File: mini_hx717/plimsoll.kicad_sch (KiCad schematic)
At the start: 17 parts, among them J1 Conn_02x06_Odd_Even, J3 Loadd Cell, U5 RS3236-3.3, U6 HX717

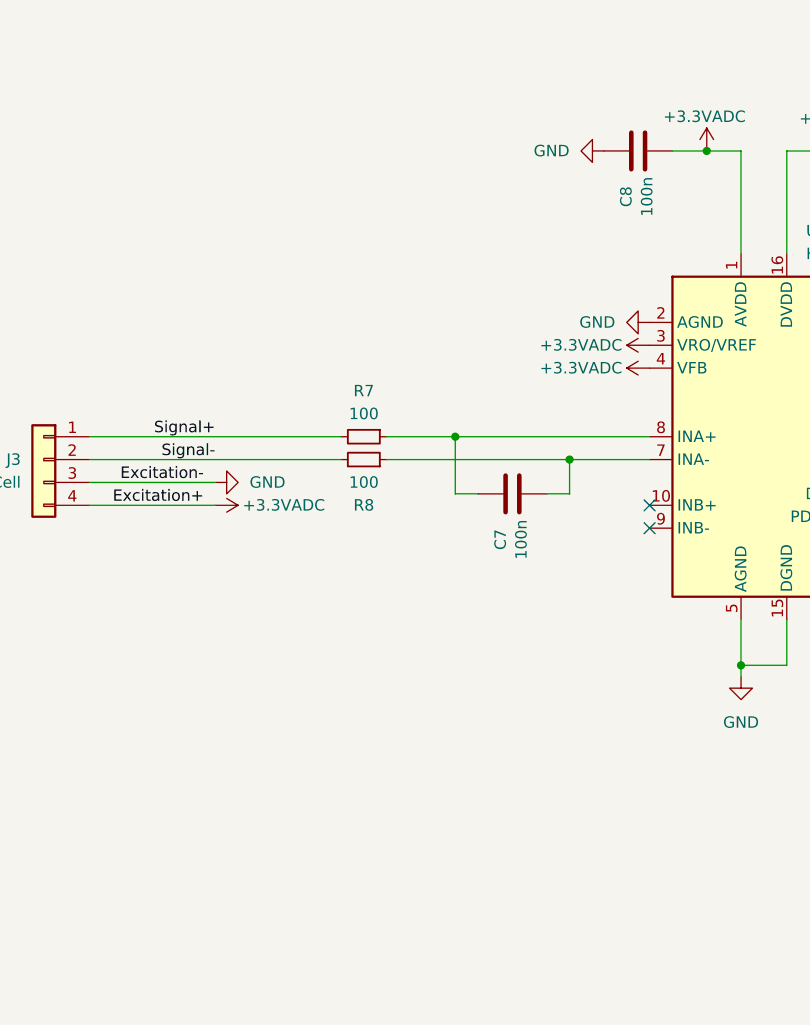
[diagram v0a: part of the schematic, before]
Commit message: ads1220 added
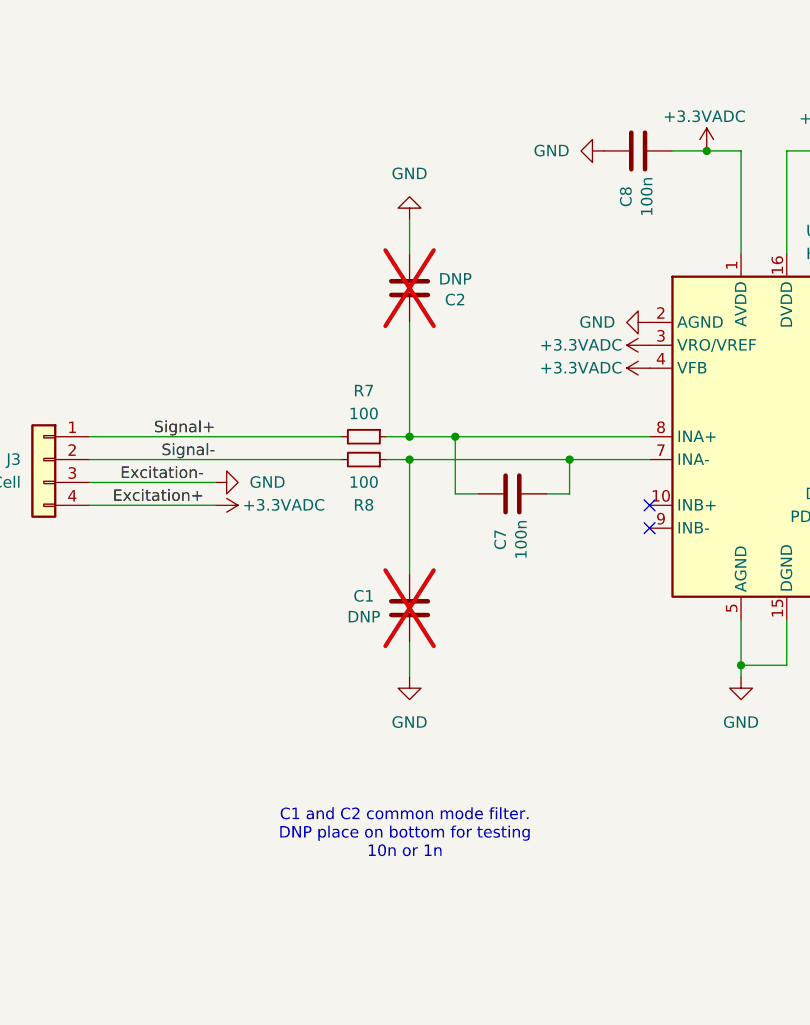
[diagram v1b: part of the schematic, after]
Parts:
- added C1, C2: DNP, Capacitor_SMD:C_0603_1608Metric, symbol Device:C
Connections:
- net GND: now also C1.1, C2.1
- net at C7.1, R8.1, U6.7 (INA-): now also C1.2
- net at C7.2, R7.1, U6.8 (INA+): now also C2.2
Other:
- note added: "C1 and C2 common mode filter. DNP place on bottom for testing 10n or 1n"

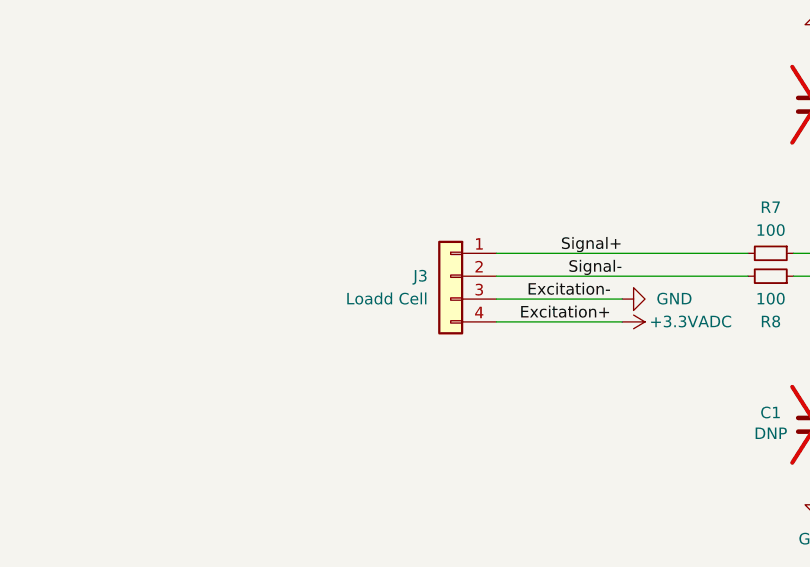
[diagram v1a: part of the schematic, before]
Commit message: Rewire connector pins and update silkscreen labels
Reassigned connector pin nets to match new signal mapping, updated silkscreen text to reflect the new pin order, and adjusted related PCB traces and vias. Also made minor component placement tweaks and cleaned up net routing for improved clarity and accuracy.
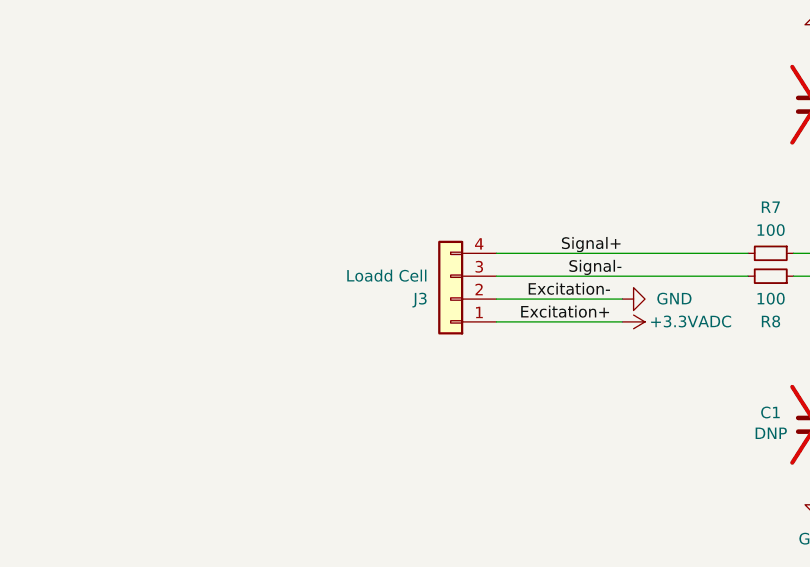
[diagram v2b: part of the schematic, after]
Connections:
- net +3.3VADC: now also J3.1 (Pin_1); no longer J3.4 (Pin_4)
- net GND: now also J3.2 (Pin_2); no longer J3.3 (Pin_3)
- net Signal+: now also J3.4 (Pin_4); no longer J3.1 (Pin_1)
- net Signal-: now also J3.3 (Pin_3); no longer J3.2 (Pin_2)
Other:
- moved on the sheet: J3
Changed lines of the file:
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@@
 	(symbol
 		(lib_id "Connector_Generic:Conn_01x04")
-		(at 210.82 138.43 0)
-		(mirror y)
+		(at 210.82 140.97 180)
 		(unit 1)
 		(exclude_from_sim no)
@@
 		(dnp no)
 		(property "Reference" "J3"
-			(at 208.28 138.4299 0)
+			(at 208.28 140.9701 0)
 			(effects
 				(font
@@
 		)
 		(property "Value" "Loadd Cell"
-			(at 208.28 140.9699 0)
+			(at 208.28 138.4301 0)
 			(effects
 				(font
@@
 		)
 		(property "Footprint" "Connector_JST:JST_XH_B4B-XH-A_1x04_P2.50mm_Vertical"
-			(at 210.82 138.43 0)
+			(at 210.82 140.97 0)
 			(effects
 				(font
@@
 		)
 		(property "Datasheet" "~"
-			(at 210.82 138.43 0)
+			(at 210.82 140.97 0)
 			(effects
 				(font
@@
 		)
 		(property "Description" "Generic connector, single row, 01x04, script generated (kicad-library-utils/schlib/autogen/connector/)"
-			(at 210.82 138.43 0)
+			(at 210.82 140.97 0)
 			(effects
 				(font
